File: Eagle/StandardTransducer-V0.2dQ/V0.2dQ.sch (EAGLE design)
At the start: 72 parts, among them CON1 SPI, IC2 TL072D, IC3 LP298XS, IC4 LORA-RA_01_SOIC, J1 87758-0216, Q1 FDN360P, Q2 FDN360P, Q3 FDN360P, Q5 BSP75, U1 RN2483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

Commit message: New version of 0.2dQ
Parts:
- removed C6: 0.1uF, rcl:C-EUC0805
- removed L2: 10uH, rcl:L-EUL1812
- added Q4: FDN360P, transistor-power:FDN360P
- added R14: 1k, rcl:R-EU_R0805
- added R19: 220k, rcl:R-EU_R0805
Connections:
- removed net A3: U$4.PF4(ADC4/TCK)
- removed net DVCC: C6.1, L2.2, Q3.S, R10.1, R11.2, R12.2, R18.2, R8.1
- removed net N$1: F1.2, L1.1, L2.1
- new net AVCCOPA: IC2P.V+, Q4.D
- new net N$3: Q4.G, R14.1, R19.1
- new net VIN: C11.1, F1.2, IC3.VIN, J1-2.S, L1.1, R10.1, R11.2, R12.2, R8.1
- net ANGND: now also IC4.GND@1, IC4.GND@3, JP5.4
- net AVCC: now also Q4.S, R19.2; no longer IC2P.V+
- net D+3V3: now also Q3.S, R18.2, U$4.PF4(ADC4/TCK)
- net D10*: now also U$4.PC6(OC3A/!OC4A); no longer U$4.PB6(OC1B/OC4B/ADC13)
- net D6*: now also U$4.PB4(ADC11); no longer U$4.PD7(OC4D/ADC10/T0)
- net D7*: now also U$4.PD7(OC4D/ADC10/T0); no longer U$4.PE6(INT.6/AIN0)
- net D8*: now also U$4.PB5(OC1A/ADC12/!OC4B); no longer U$4.PB4(ADC11)
- net D9*: now also U$4.PB6(OC1B/OC4B/ADC13); no longer U$4.PB5(OC1A/ADC12/!OC4B)
- net GND: no longer C6.2, IC4.GND@1, IC4.GND@3, JP5.4
- net RA1/2483: now also U$4.PE6(INT.6/AIN0); no longer U$4.PC6(OC3A/!OC4A)
- net VCC: no longer C11.1, IC3.VIN, J1-2.S
- net VOPA: now also R14.2
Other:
- note added: "Se cambia por un LP5907 que entrega 250 mA."
- moved on the sheet: C4, F1, L1

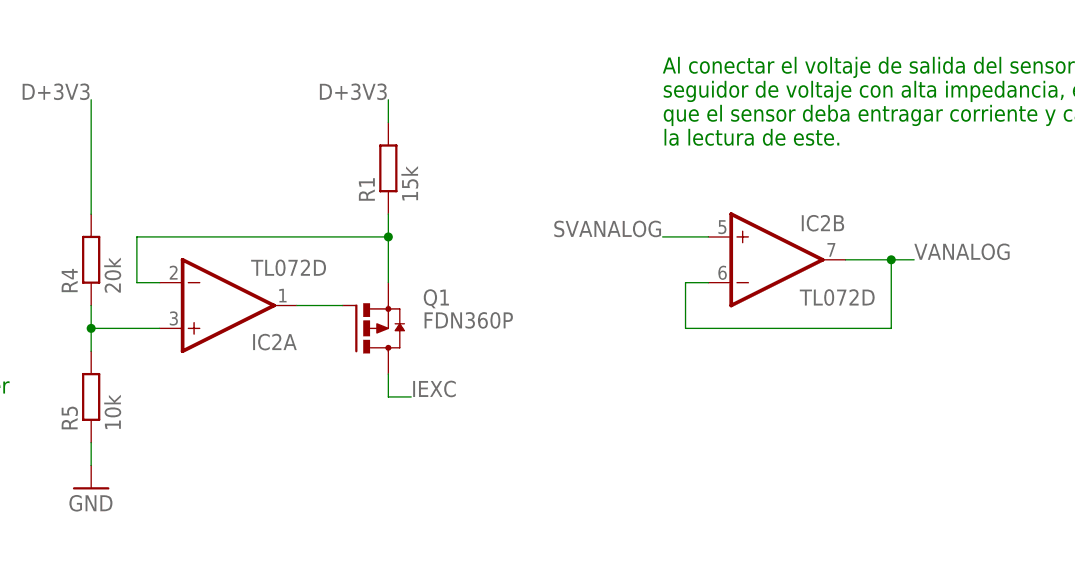
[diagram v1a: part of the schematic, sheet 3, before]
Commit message: Changes width for VCCOPA and SVANALOG
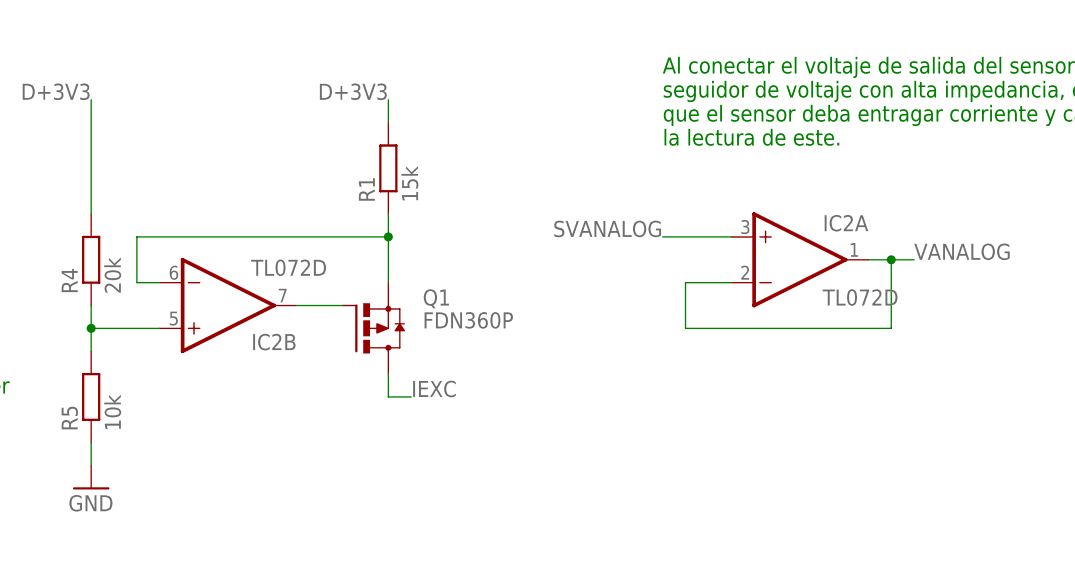
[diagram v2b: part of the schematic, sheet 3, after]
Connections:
- removed net N$2: IC2A.OUT, Q1.G
- new net N$1: IC2B.OUT, Q1.G
- net N$4: now also IC2B.+IN; no longer IC2A.+IN
- net N$5: now also IC2B.-IN; no longer IC2A.-IN
- net SVANALOG: now also IC2A.+IN; no longer IC2B.+IN
- net VANALOG: now also IC2A.-IN, IC2A.OUT; no longer IC2B.-IN, IC2B.OUT
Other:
- moved on the sheet: IC2A, IC2B
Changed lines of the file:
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@@
 <instance part="R18" gate="G$1" x="279.4" y="134.62" rot="R90"/>
 <instance part="Q3" gate="G$1" x="284.48" y="121.92"/>
-<instance part="IC2" gate="A" x="281.94" y="55.88" rot="MR180"/>
-<instance part="IC2" gate="B" x="342.9" y="60.96"/>
+<instance part="IC2" gate="A" x="345.44" y="60.96"/>
+<instance part="IC2" gate="B" x="281.94" y="55.88" rot="MR180"/>
 <instance part="IC2" gate="P" x="353.06" y="0" rot="R90"/>
 <instance part="Q1" gate="G$1" x="297.18" y="53.34"/>
@@
 </segment>
 <segment>
-<pinref part="IC2" gate="B" pin="OUT"/>
-<wire x1="350.52" y1="60.96" x2="355.6" y2="60.96" width="0.1524" layer="91"/>
 <wire x1="355.6" y1="60.96" x2="355.6" y2="53.34" width="0.1524" layer="91"/>
 <wire x1="355.6" y1="53.34" x2="332.74" y2="53.34" width="0.1524" layer="91"/>
-<pinref part="IC2" gate="B" pin="-IN"/>
 <wire x1="332.74" y1="53.34" x2="332.74" y2="58.42" width="0.1524" layer="91"/>
-<wire x1="332.74" y1="58.42" x2="335.28" y2="58.42" width="0.1524" layer="91"/>
 <wire x1="355.6" y1="60.96" x2="358.14" y2="60.96" width="0.1524" layer="91"/>
 <label x="358.14" y="60.96" size="1.778" layer="95"/>
+<pinref part="IC2" gate="A" pin="-IN"/>
+<wire x1="337.82" y1="58.42" x2="332.74" y2="58.42" width="0.1524" layer="91"/>
+<pinref part="IC2" gate="A" pin="OUT"/>
+<wire x1="353.06" y1="60.96" x2="355.6" y2="60.96" width="0.1524" layer="91"/>
 <junction x="355.6" y="60.96"/>
 </segment>
@@
 </segment>
 </net>
-<net name="N$2" class="0">
-<segment>
-<pinref part="Q1" gate="G$1" pin="G"/>
-<pinref part="IC2" gate="A" pin="OUT"/>
-<wire x1="294.64" y1="55.88" x2="289.56" y2="55.88" width="0.1524" layer="91"/>
-</segment>
-</net>
 <net name="N$5" class="0">
 <segment>
@@
 <pinref part="Q1" gate="G$1" pin="S"/>
 <wire x1="299.72" y1="66.04" x2="299.72" y2="63.5" width="0.1524" layer="91"/>
-<pinref part="IC2" gate="A" pin="-IN"/>
 <wire x1="299.72" y1="63.5" x2="299.72" y2="58.42" width="0.1524" layer="91"/>
-<wire x1="274.32" y1="58.42" x2="271.78" y2="58.42" width="0.1524" layer="91"/>
 <wire x1="271.78" y1="58.42" x2="271.78" y2="63.5" width="0.1524" layer="91"/>
 <wire x1="271.78" y1="63.5" x2="299.72" y2="63.5" width="0.1524" layer="91"/>
 <junction x="299.72" y="63.5"/>
+<pinref part="IC2" gate="B" pin="-IN"/>
+<wire x1="274.32" y1="58.42" x2="271.78" y2="58.42" width="0.1524" layer="91"/>
 </segment>
 </net>
 <net name="N$4" class="0">
 <segment>
-<pinref part="IC2" gate="A" pin="+IN"/>
 <pinref part="R5" gate="G$1" pin="2"/>
-<wire x1="274.32" y1="53.34" x2="266.7" y2="53.34" width="0.1524" layer="91"/>
-<wire x1="266.7" y1="53.34" x2="266.7" y2="50.8" width="0.1524" layer="91"/>
 <pinref part="R4" gate="G$1" pin="1"/>
 <wire x1="266.7" y1="55.88" x2="266.7" y2="53.34" width="0.1524" layer="91"/>
+<pinref part="IC2" gate="B" pin="+IN"/>
+<wire x1="266.7" y1="53.34" x2="266.7" y2="50.8" width="0.1524" layer="91"/>
+<wire x1="274.32" y1="53.34" x2="266.7" y2="53.34" width="0.1524" layer="91"/>
 <junction x="266.7" y="53.34"/>
 </segment>
 </net>
 <net name="SVANALOG" class="0">
-<segment>
-<pinref part="IC2" gate="B" pin="+IN"/>
-<wire x1="335.28" y1="63.5" x2="330.2" y2="63.5" width="0.1524" layer="91"/>
-<label x="330.2" y="63.5" size="1.778" layer="95" rot="MR0"/>
-</segment>
 <segment>
 <label x="152.4" y="152.4" size="1.778" layer="95" rot="MR0"/>
 <wire x1="170.18" y1="152.4" x2="152.4" y2="152.4" width="0.1524" layer="91"/>
 <pinref part="JP4" gate="A" pin="7"/>
+</segment>
+<segment>
+<pinref part="IC2" gate="A" pin="+IN"/>
+<wire x1="337.82" y1="63.5" x2="330.2" y2="63.5" width="0.1524" layer="91"/>
+<label x="330.2" y="63.5" size="1.778" layer="95" rot="MR0"/>
 </segment>
 </net>
@@
 </segment>
 </net>
+<net name="N$1" class="0">
+<segment>
+<pinref part="IC2" gate="B" pin="OUT"/>
+<pinref part="Q1" gate="G$1" pin="G"/>
+<wire x1="289.56" y1="55.88" x2="294.64" y2="55.88" width="0.1524" layer="91"/>
+</segment>
+</net>

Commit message: EN pin of LP298SX is connect to VIN pin.
- Delete sheets 2, 3 and 4 and paste all the components and connections to sheet 1.
- EN pin is connect to VIN pin for LP298SX to ensure that microcontroller have power source.
- Change width for all route of D+3V3.
- Change conections for TL072D to minimize route and vias for SVANALOG.
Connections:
- net ENREG: no longer IC3.EN
- net VIN: now also IC3.EN
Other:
- note added: "COMMUNICATION"
- note added: "En este caso, para evitar que el regulador no se encienda, el pin EN se conecta directamente a la alimentación."
- note added: "Fuente de corriente."
- note added: "Habilitación de la fuente de alimentación para los sensores análogos."
- note removed: "Connections for antennas"

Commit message: Update ICs and routes.
Changes made:
- BSP75 (BSP613P) to BSP75N.
- FDN 360P to FDN340P (logic level).
- LP298SX to LP5907 (250 mA).
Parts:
- removed C12: 10nF, rcl:C-EUC0805
- IC3: value LP298XS -> LP5907; device adafruit:LP298XS -> LP5907:LP5907
- Q1, Q2, Q3, Q4: value FDN360P -> FDN340P; device transistor-power:FDN360P -> FDN340P:FDN340P
- Q5: value BSP75 -> BSP75N; device infineon:BSP613P -> BSP75N:BSP75N
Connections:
- removed net N$6: C12.1, IC3.BYP
- net GND: no longer C12.2
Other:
- note removed: "Se cambia por un LP5907 que entrega 250 mA."
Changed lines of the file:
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@@
 <part name="J2" library="SparkFun-Connectors" deviceset="CONN_02" device=""/>
 <part name="F1" library="adafruit" library_urn="urn:adsk.eagle:library:420" deviceset="PTCFUSE" device="-1812" value="1A"/>
-<part name="Q1" library="transistor-power" library_urn="urn:adsk.eagle:library:400" deviceset="FDN360P" device="" package3d_urn="urn:adsk.eagle:package:29529/2"/>
+<part name="Q1" library="FDN340P" deviceset="FDN340P" device=""/>
 <part name="R1" library="rcl" library_urn="urn:adsk.eagle:library:334" deviceset="R-EU_" device="R0805" package3d_urn="urn:adsk.eagle:package:23553/2" value="15k"/>
-<part name="IC3" library="adafruit" library_urn="urn:adsk.eagle:library:420" deviceset="LP298X" device="S"/>
+<part name="IC3" library="LP5907" deviceset="LP5907" device=""/>
 <part name="C11" library="rcl" library_urn="urn:adsk.eagle:library:334" deviceset="C-EU" device="C0805" package3d_urn="urn:adsk.eagle:package:23617/2" value="1uF"/>
 <part name="GND6" library="supply1" deviceset="GND" device=""/>
 <part name="GND7" library="supply1" deviceset="GND" device=""/>
-<part name="C12" library="rcl" library_urn="urn:adsk.eagle:library:334" deviceset="C-EU" device="C0805" package3d_urn="urn:adsk.eagle:package:23617/2" value="10nF"/>
 <part name="C13" library="rcl" library_urn="urn:adsk.eagle:library:334" deviceset="C-EU" device="C0805" package3d_urn="urn:adsk.eagle:package:23617/2" value="2.2uF"/>
-<part name="GND8" library="supply1" deviceset="GND" device=""/>
 <part name="GND9" library="supply1" deviceset="GND" device=""/>
 <part name="C1" library="rcl" library_urn="urn:adsk.eagle:library:334" deviceset="C-EU" device="C0805" package3d_urn="urn:adsk.eagle:package:23617/2" value="100nF"/>
@@
 <part name="R5" library="rcl" library_urn="urn:adsk.eagle:library:334" deviceset="R-EU_" device="R0805" package3d_urn="urn:adsk.eagle:package:23553/2" value="10k"/>
 <part name="GND11" library="supply1" deviceset="GND" device=""/>
-<part name="Q2" library="transistor-power" library_urn="urn:adsk.eagle:library:400" deviceset="FDN360P" device="" package3d_urn="urn:adsk.eagle:package:29529/2"/>
+<part name="Q2" library="FDN340P" deviceset="FDN340P" device=""/>
 <part name="R6" library="rcl" library_urn="urn:adsk.eagle:library:334" deviceset="R-EU_" device="R0805" package3d_urn="urn:adsk.eagle:package:23553/2" value="1k"/>
 <part name="R7" library="rcl" library_urn="urn:adsk.eagle:library:334" deviceset="R-EU_" device="R0805" package3d_urn="urn:adsk.eagle:package:23553/2" value="220k"/>
 <part name="R16" library="rcl" library_urn="urn:adsk.eagle:library:334" deviceset="R-EU_" device="R0805" package3d_urn="urn:adsk.eagle:package:23553/2" value="1k"/>
 <part name="R18" library="rcl" library_urn="urn:adsk.eagle:library:334" deviceset="R-EU_" device="R0805" package3d_urn="urn:adsk.eagle:package:23553/2" value="220k"/>
-<part name="Q3" library="transistor-power" library_urn="urn:adsk.eagle:library:400" deviceset="FDN360P" device="" package3d_urn="urn:adsk.eagle:package:29529/2"/>
+<part name="Q3" library="FDN340P" deviceset="FDN340P" device=""/>
 <part name="SJ4" library="jumper" library_urn="urn:adsk.eagle:library:252" deviceset="SJ" device="" package3d_urn="urn:adsk.eagle:package:15471/1"/>
 <part name="GND13" library="supply1" deviceset="GND" device=""/>
 <part name="SJ5" library="jumper" library_urn="urn:adsk.eagle:library:252" deviceset="SJ" device="" package3d_urn="urn:adsk.eagle:package:15471/1"/>
-<part name="Q5" library="infineon" deviceset="BSP613P" device="" value="BSP75"/>
 <part name="GND17" library="supply1" deviceset="GND" device=""/>
 <part name="RK6" library="resistor" deviceset="R-EU_" device="M0805" value="10k"/>
-<part name="Q4" library="transistor-power" library_urn="urn:adsk.eagle:library:400" deviceset="FDN360P" device="" package3d_urn="urn:adsk.eagle:package:29529/2"/>
+<part name="Q4" library="FDN340P" deviceset="FDN340P" device=""/>
 <part name="R14" library="rcl" library_urn="urn:adsk.eagle:library:334" deviceset="R-EU_" device="R0805" package3d_urn="urn:adsk.eagle:package:23553/2" value="1k"/>
 <part name="R19" library="rcl" library_urn="urn:adsk.eagle:library:334" deviceset="R-EU_" device="R0805" package3d_urn="urn:adsk.eagle:package:23553/2" value="220k"/>
 <part name="FRAME3" library="frames" library_urn="urn:adsk.eagle:library:229" deviceset="TABL_L" device=""/>
+<part name="Q5" library="BSP75N" deviceset="BSP75N" device=""/>
 </parts>
 <sheets>
@@
 - ISP+5V: Puerto ISP del programador.</text>
 <text x="137.16" y="246.38" size="1.778" layer="91">Power source for communication</text>
-<text x="147.32" y="205.74" size="1.778" layer="91">Se cambia por un
-LP5907 que entrega
-250 mA.</text>
 <text x="134.62" y="195.58" size="1.778" layer="91">En este caso, para evitar que el regulador no se
 encienda, el pin EN se conecta directamente a la
@@
 <instance part="GND13" gate="1" x="297.18" y="111.76"/>
 <instance part="SJ5" gate="1" x="299.72" y="177.8"/>
-<instance part="Q5" gate="G$1" x="129.54" y="17.78"/>
 <instance part="GND17" gate="1" x="132.08" y="5.08"/>
 <instance part="RK6" gate="G$1" x="124.46" y="10.16"/>
@@
 <attribute name="VALUE" x="135.255" y="206.375" size="1.27" layer="96"/>
 </instance>
-<instance part="C12" gate="G$1" x="172.72" y="218.44"/>
 <instance part="C13" gate="G$1" x="182.88" y="218.44"/>
-<instance part="GND8" gate="1" x="172.72" y="208.28" smashed="yes">
-<attribute name="VALUE" x="170.815" y="206.375" size="1.27" layer="96"/>
-</instance>
 <instance part="GND9" gate="1" x="182.88" y="208.28" smashed="yes">
 <attribute name="VALUE" x="180.975" y="206.375" size="1.27" layer="96"/>
@@
 <instance part="+3V2" gate="G$1" x="10.16" y="182.88"/>
 <instance part="JP2" gate="G$1" x="25.4" y="175.26"/>
+<instance part="Q5" gate="G$1" x="129.54" y="17.78"/>
 </instances>
 <busses>
@@
 </segment>
 <segment>
-<pinref part="Q5" gate="G$1" pin="S"/>
 <wire x1="132.08" y1="12.7" x2="132.08" y2="10.16" width="0.1524" layer="91"/>
 <pinref part="GND17" gate="1" pin="GND"/>
@@
 <wire x1="129.54" y1="10.16" x2="132.08" y2="10.16" width="0.1524" layer="91"/>
 <junction x="132.08" y="10.16"/>
+<pinref part="Q5" gate="G$1" pin="S"/>
 </segment>
 <segment>
@@
 <pinref part="GND7" gate="1" pin="GND"/>
 <wire x1="137.16" y1="213.36" x2="137.16" y2="210.82" width="0.1524" layer="91"/>
-</segment>
-<segment>
-<pinref part="C12" gate="G$1" pin="2"/>
-<pinref part="GND8" gate="1" pin="GND"/>
-<wire x1="172.72" y1="213.36" x2="172.72" y2="210.82" width="0.1524" layer="91"/>
 </segment>
 <segment>
@@
 <net name="D7*" class="0">
 <segment>
-<pinref part="Q5" gate="G$1" pin="G"/>
 <wire x1="127" y1="15.24" x2="119.38" y2="15.24" width="0.1524" layer="91"/>
 <wire x1="116.84" y1="15.24" x2="119.38" y2="15.24" width="0.1524" layer="91"/>
@@
 <junction x="119.38" y="15.24"/>
 <label x="116.84" y="15.24" size="1.778" layer="95" rot="MR0"/>
+<pinref part="Q5" gate="G$1" pin="G"/>
 </segment>
 <segment>
@@
 <net name="ANGND" class="0">
 <segment>
-<pinref part="Q5" gate="G$1" pin="D@1"/>
 <wire x1="132.08" y1="25.4" x2="132.08" y2="22.86" width="0.1524" layer="91"/>
 <wire x1="132.08" y1="25.4" x2="134.62" y2="25.4" width="0.1524" layer="91"/>
@@
 <label x="134.62" y="25.4" size="1.778" layer="95"/>
 <junction x="132.08" y="25.4"/>
+<pinref part="Q5" gate="G$1" pin="D@1"/>
 </segment>
 <segment>
@@
 </segment>
 </net>
-<net name="N$6" class="0">
-<segment>
-<pinref part="IC3" gate="G$1" pin="BYP"/>
-<pinref part="C12" gate="G$1" pin="1"/>
-<wire x1="170.18" y1="223.52" x2="172.72" y2="223.52" width="0.1524" layer="91"/>
-<wire x1="172.72" y1="223.52" x2="172.72" y2="220.98" width="0.1524" layer="91"/>
-</segment>
-</net>
